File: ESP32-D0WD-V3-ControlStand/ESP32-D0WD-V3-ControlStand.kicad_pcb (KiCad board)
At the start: 2 copper layers, 198.1 x 126.4 mm, 196 parts, among them J1 Button & LED Panel, J10 RJ45, J11 Barrel_Jack, J12 Battery, J13 USB_OTG, J2 Button & LED Panel, J3 STEMMA (Display), J4 Horn, J5 Brake, J6 Light Switch, J7 Reverser, J8 Throttle, J9 RJ45, P1 CONN_8, P2 Misc buttons, bell, status LED, P6 CONN_3, P7 CONN_3, P8 CONN_5, P9 CONN_5, Q1 UMH3N, SW1 A, SW10 SW_PUSH_SMALL, SW11 SW_PUSH_SMALL, SW12 SW_PUSH_SMALL, SW13 SW_PUSH_SMALL, SW14 SW_PUSH_SMALL, SW15 SW_PUSH_SMALL, SW16 SW_PUSH_SMALL, SW17 SW_PUSH_SMALL, SW18 SW_PUSH_SMALL, SW19 SW_PUSH_SMALL, SW2 B, SW20 SW_PUSH_SMALL, SW21 SW_PUSH_SMALL, SW22 SW_PUSH_SMALL, SW23 On/Off, SW24 RESET, SW3 C, SW4 D, SW5 Bell, SW7 SW_PUSH_SMALL, SW8 SW_PUSH_SMALL, SW9 SW_PUSH_SMALL, T1 Buttons, T2 LEDS, T3 Buttons, T4 LEDS, T5 + 15 in -, T6 + 15 out -, U1 MCP23017, U10 ESP32-D0WD-V3, U11 W25Q32JVSSIQ, U2 TBD62083A, U3 MCP23017, U4 TBD62083A, U5 TCAN332DR, U6 MCP73871, U7 LM2574HVM-5.0, U8 TC1263-3.3VOATR, U9 FT231XS-R, Y1 40 Mhz +/- 10 ppm

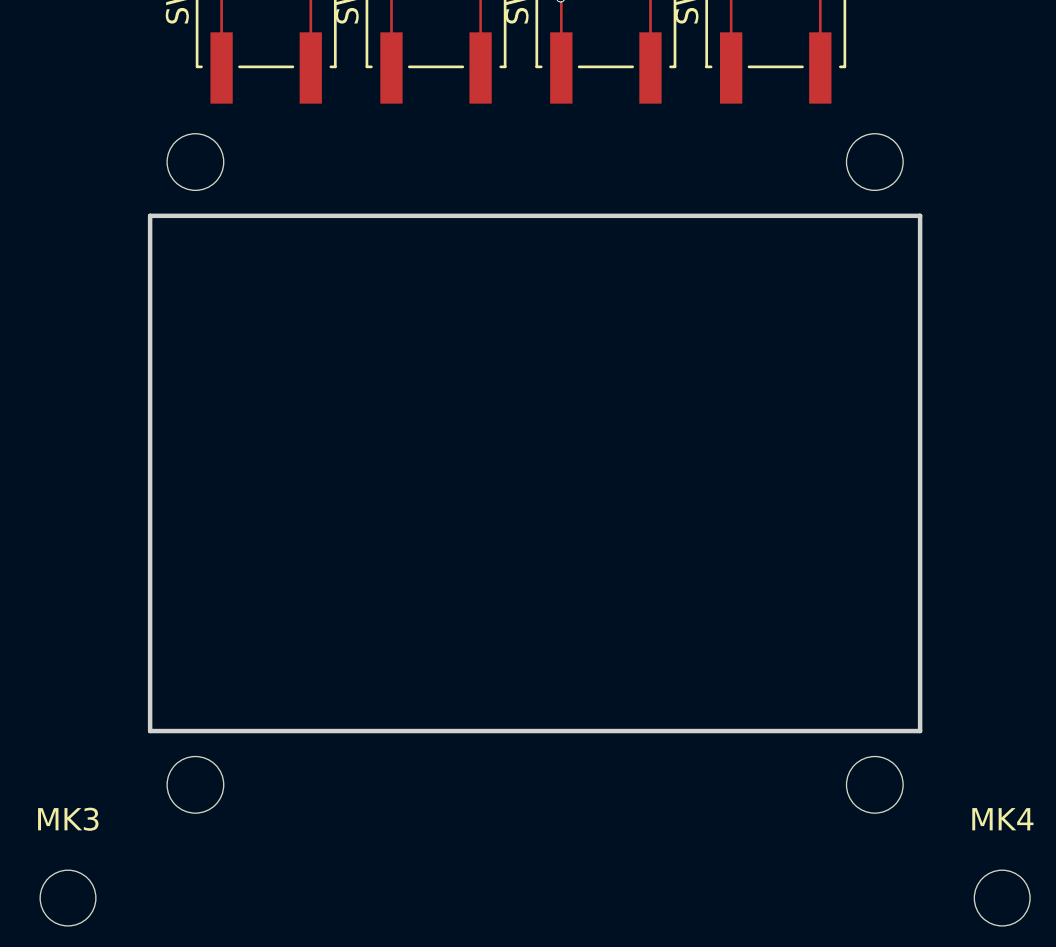
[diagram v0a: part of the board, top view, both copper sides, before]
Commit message: Working on CAD: handheld box.
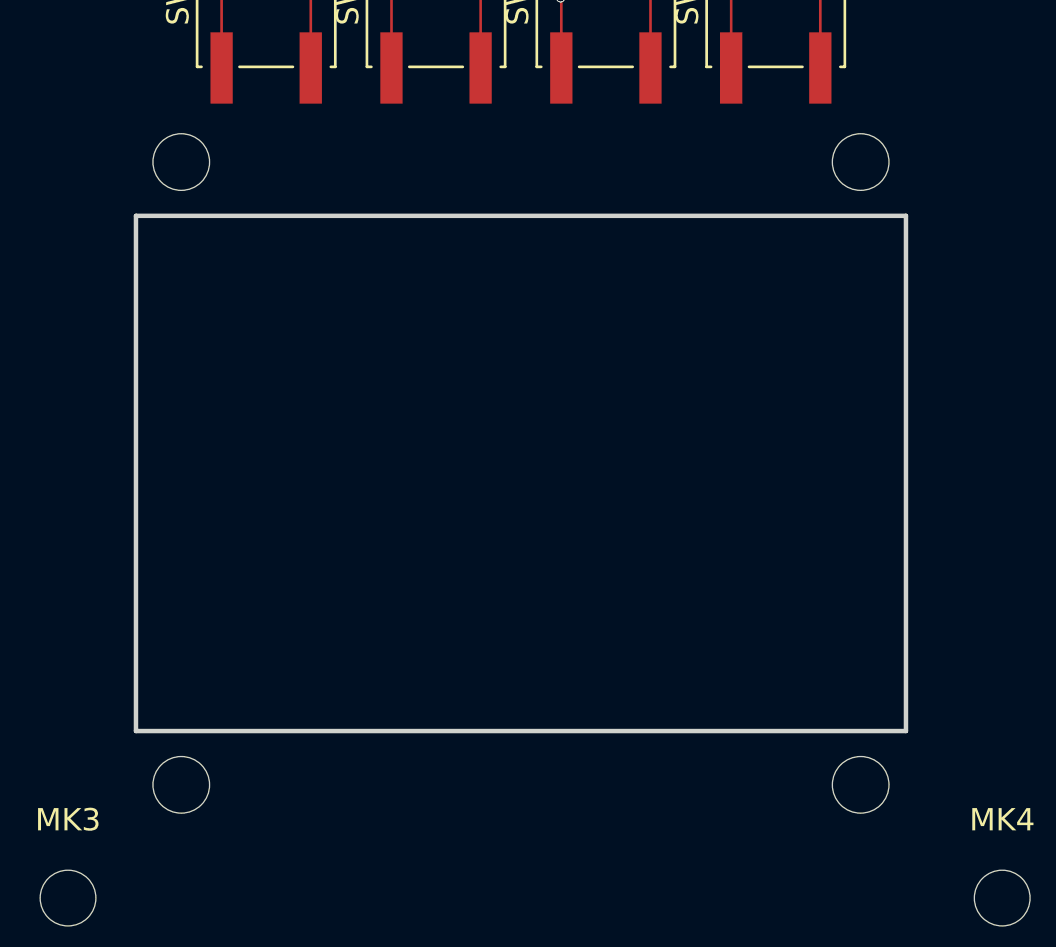
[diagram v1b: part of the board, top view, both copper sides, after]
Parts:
- moved REF** 0.63 mm to (76.2, 77.5)
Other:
- outline, holes or cut-outs redrawn
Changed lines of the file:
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@@
     (area 11.176 11.1125 286.448501 198.628001)
     (thickness 1.6)
-    (drawings 93)
+    (drawings 92)
     (tracks 1896)
     (zones 0)
@@
   )
   (module AdafruitDisplays:128x64OLEDSTEMMA locked (layer F.Cu)
-    (at 76.835 77.47 180)
+    (at 76.2 77.47 180)
     (fp_text reference REF** (at 0.0381 -15.3797 180) (layer B.SilkS)
       (effects (font (size 1 1) (thickness 0.15)) (justify mirror))
@@
   (gr_line (start 113.03 25.4) (end 163.83 25.4) (layer Edge.Cuts) (width 0.2))
   (gr_line (start 113.03 97.79) (end 113.03 25.4) (layer Edge.Cuts) (width 0.2))
-  (gr_line (start 94.107 63.373) (end 94.107 86.487) (layer Edge.Cuts) (width 0.2))
-  (gr_line (start 59.563 63.373) (end 94.107 63.373) (layer Edge.Cuts) (width 0.2))
-  (gr_line (start 59.563 86.487) (end 59.563 63.373) (layer Edge.Cuts) (width 0.2))
-  (gr_line (start 94.107 86.487) (end 59.563 86.487) (layer Edge.Cuts) (width 0.2))
-  (gr_line (start 50.8 97.79) (end 101.6 97.79) (layer Dwgs.User) (width 0.2))
+  (gr_line (start 93.472 63.373) (end 93.472 86.487) (layer Edge.Cuts) (width 0.2))
+  (gr_line (start 58.928 63.373) (end 93.472 63.373) (layer Edge.Cuts) (width 0.2))
+  (gr_line (start 58.928 86.487) (end 58.928 63.373) (layer Edge.Cuts) (width 0.2))
+  (gr_line (start 93.472 86.487) (end 58.928 86.487) (layer Edge.Cuts) (width 0.2))
   (gr_line (start 94.869 100.965) (end 110.49 100.965) (layer Edge.Cuts) (width 0.2))
   (gr_line (start 94.869 97.79) (end 94.869 100.965) (layer Edge.Cuts) (width 0.2))

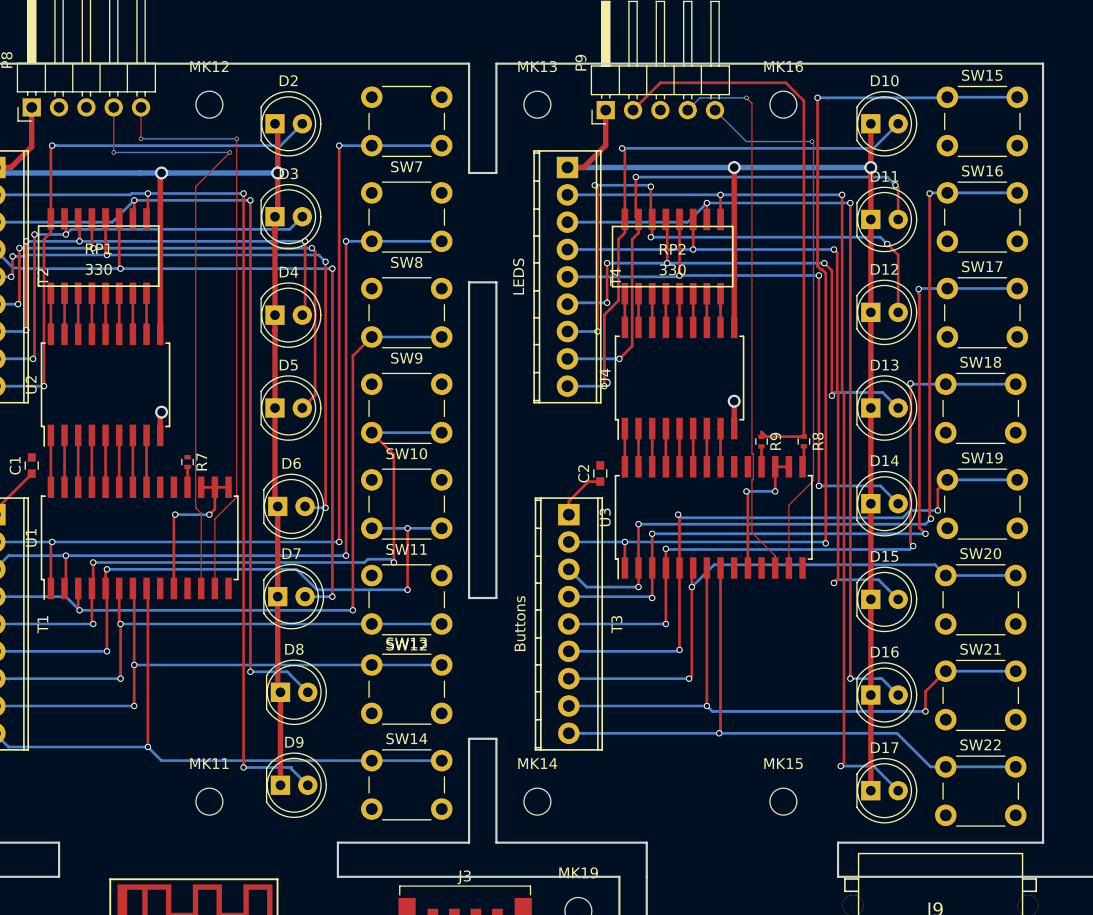
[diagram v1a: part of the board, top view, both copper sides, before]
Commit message: Working on CAD models.
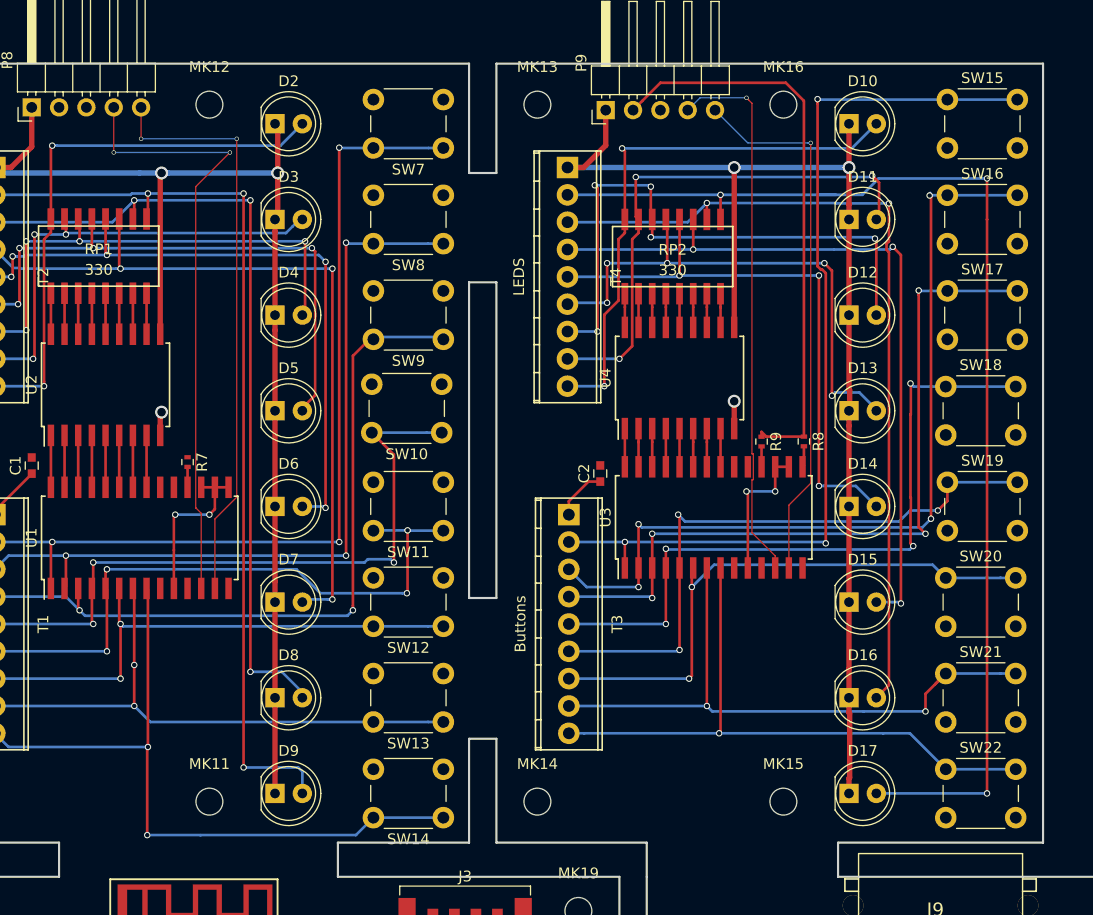
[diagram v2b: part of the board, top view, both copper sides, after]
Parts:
- moved SW13 8.50 mm to (161.4, 86.6), turned to 180 degrees
- moved SW14 8.50 mm to (161.4, 95.5), turned to 180 degrees
- moved D14 2.05 mm to (199.1, 66.5)
- moved D15 2.05 mm to (199.1, 75.4)
- moved D16 2.05 mm to (199.1, 84.3)
- moved D17 2.05 mm to (199.1, 93.2)
- moved D12 2.05 mm to (199.1, 48.8)
- moved D13 2.05 mm to (199.1, 57.7)
- moved D10 2.03 mm to (199.1, 31.0)
- moved D11 2.03 mm to (199.1, 39.9)
- moved D9 0.92 mm to (145.8, 93.2)
- moved D8 0.72 mm to (145.8, 84.3)
- moved D7 0.57 mm to (145.8, 75.4)
- moved SW11 0.26 mm to (161.4, 68.8)
- moved SW12 0.26 mm to (161.4, 77.7)
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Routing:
- net Net-(D17-Pad2): track 87.4 -> 111.1 mm
- net Net-(SW14-Pad1): track 57.4 -> 65.9 mm, vias 1 -> 2
- net Net-(D15-Pad2): track 65.7 -> 69.1 mm
- net Net-(D10-Pad2): track 53.0 -> 51.0 mm
- net Net-(D13-Pad2): track 51.2 -> 49.2 mm
- net Net-(D14-Pad2): track 56.2 -> 54.3 mm
- net +BATT: track 224.0 -> 222.2 mm
- net Net-(D11-Pad2): track 50.3 -> 48.9 mm
- net Net-(SW21-Pad1): track 57.2 -> 58.4 mm
- net Net-(D16-Pad2): track 77.8 -> 78.8 mm, vias 3 -> 2
- net Net-(D12-Pad2): track 55.6 -> 54.6 mm
- net Net-(SW13-Pad1): track 52.5 -> 53.3 mm
- net Net-(SW15-Pad1): track 86.7 -> 87.3 mm
- net Net-(SW10-Pad1): vias 4 -> 3
